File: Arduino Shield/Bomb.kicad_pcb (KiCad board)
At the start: 2 copper layers, 27.9 x 21.6 mm, 6 parts, among them J1 Digital/PWM, J2 I2C Out, J3 Power, J4 Logic, U1 ATtiny85

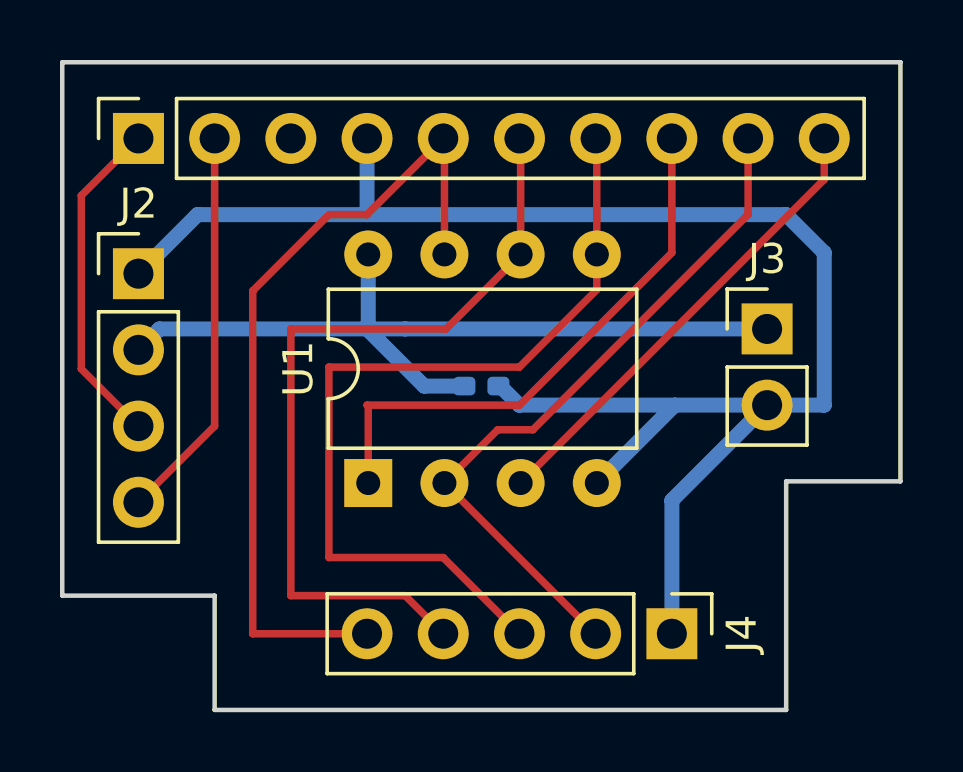
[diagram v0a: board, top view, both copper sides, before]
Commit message: Widened the pads of C1 in the arduino shield, switched the pinout of the i2c out, adjusted the size of the arduino shield board
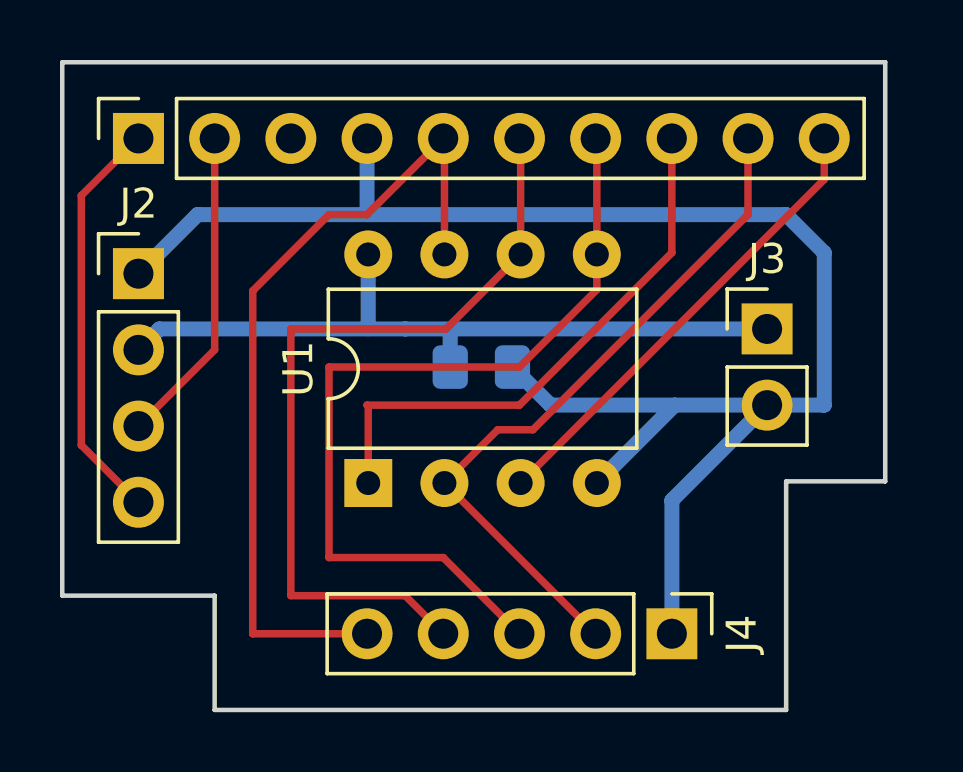
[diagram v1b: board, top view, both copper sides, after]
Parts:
- C1: footprint Capacitor_SMD:C_0402_1005Metric_Pad0.74x0.62mm_HandSolder -> Capacitor_SMD:C_0805_2012Metric_Pad1.18x1.45mm_HandSolder
- moved C1 0.63 mm to (129.2, 56.8)
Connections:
- J2 pad 3: /SCL/A5 -> /SDA/A4
- J2 pad 4: /SDA/A4 -> /SCL/A5
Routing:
- net +5V: track 27.7 -> 25.0 mm
- net /SDA/A4: track 13.2 -> 10.6 mm
- net /SCL/A5: track 11.2 -> 13.7 mm
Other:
- board size 27.9 x 21.6 mm -> 27.4 x 21.6 mm
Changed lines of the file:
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@@
       (net 2 "+5V") (pinfunction "Pin_2") (pintype "passive"))
     (pad "3" thru_hole oval (at 0 5.08) (size 1.7 1.7) (drill 1) (layers *.Cu *.Mask)
-      (net 4 "/SCL{slash}A5") (pinfunction "Pin_3") (pintype "passive"))
+      (net 3 "/SDA{slash}A4") (pinfunction "Pin_3") (pintype "passive"))
     (pad "4" thru_hole oval (at 0 7.62) (size 1.7 1.7) (drill 1) (layers *.Cu *.Mask)
-      (net 3 "/SDA{slash}A4") (pinfunction "Pin_4") (pintype "passive"))
+      (net 4 "/SCL{slash}A5") (pinfunction "Pin_4") (pintype "passive"))
     (model "${KICAD6_3DMODEL_DIR}/Connector_PinHeader_2.54mm.3dshapes/PinHeader_1x04_P2.54mm_Vertical.wrl"
       (offset (xyz 0 0 0))
@@
     )
   )
-  (footprint "Capacitor_SMD:C_0402_1005Metric_Pad0.74x0.62mm_HandSolder" (layer "B.Cu")
-    (at 129.21 57.455)
-    (descr "Capacitor SMD 0402 (1005 Metric), square (rectangular) end terminal, IPC_7351 nominal with elongated pad for handsoldering. (Body size source: IPC-SM-782 page 76, https://www.pcb-3d.com/wordpress/wp-content/uploads/ipc-sm-782a_amendment_1_and_2.pdf), generated with kicad-footprint-generator")
+  (footprint "Capacitor_SMD:C_0805_2012Metric_Pad1.18x1.45mm_HandSolder" (layer "B.Cu")
+    (at 129.21 56.82)
+    (descr "Capacitor SMD 0805 (2012 Metric), square (rectangular) end terminal, IPC_7351 nominal with elongated pad for handsoldering. (Body size source: IPC-SM-782 page 76, https://www.pcb-3d.com/wordpress/wp-content/uploads/ipc-sm-782a_amendment_1_and_2.pdf, https://docs.google.com/spreadsheets/d/1BsfQQcO9C6DZCsRaXUlFlo91Tg2WpOkGARC1WS5S8t0/edit?usp=sharing), generated with kicad-footprint-generator")
     (tags "capacitor handsolder")
     (property "Sheetfile" "Bomb.kicad_sch")
     (property "Sheetname" "")
     (attr smd)
-    (fp_text reference "C1" (at 0 1.16 180) (layer "B.SilkS")
+    (fp_text reference "C1" (at 0 1.68 180) (layer "B.SilkS")
       (effects (font (size 1 1) (thickness 0.15)) (justify mirror))
     )
-    (fp_text value "C" (at 0 -1.16 180) (layer "B.Fab") hide
+    (fp_text value "C" (at 0 -1.68 180) (layer "B.Fab")
       (effects (font (size 1 1) (thickness 0.15)) (justify mirror))
     )
     (fp_text user "${REFERENCE}" (at 0 0 180) (layer "B.Fab")
-      (effects (font (size 0.25 0.25) (thickness 0.04)) (justify mirror))
+      (effects (font (size 0.5 0.5) (thickness 0.08)) (justify mirror))
     )
-    (fp_line (start -0.115835 0.36) (end 0.115835 0.36) (layer "B.SilkS") (width 0.12))
-    (fp_line (start -0.115835 -0.36) (end 0.115835 -0.36) (layer "B.SilkS") (width 0.12))
-    (fp_line (start -1.08 -0.46) (end -1.08 0.46) (layer "B.CrtYd") (width 0.05))
-    (fp_line (start 1.08 0.46) (end 1.08 -0.46) (layer "B.CrtYd") (width 0.05))
-    (fp_line (start 1.08 -0.46) (end -1.08 -0.46) (layer "B.CrtYd") (width 0.05))
-    (fp_line (start -1.08 0.46) (end 1.08 0.46) (layer "B.CrtYd") (width 0.05))
-    (fp_line (start -0.5 0.25) (end 0.5 0.25) (layer "B.Fab") (width 0.1))
-    (fp_line (start 0.5 0.25) (end 0.5 -0.25) (layer "B.Fab") (width 0.1))
-    (fp_line (start 0.5 -0.25) (end -0.5 -0.25) (layer "B.Fab") (width 0.1))
-    (fp_line (start -0.5 -0.25) (end -0.5 0.25) (layer "B.Fab") (width 0.1))
-    (pad "1" smd roundrect (at -0.5675 0) (size 0.735 0.62) (layers "B.Cu" "B.Paste" "B.Mask") (roundrect_rratio 0.25)
+    (fp_line (start -0.261252 0.735) (end 0.261252 0.735) (layer "B.SilkS") (width 0.12))
+    (fp_line (start -0.261252 -0.735) (end 0.261252 -0.735) (layer "B.SilkS") (width 0.12))
+    (fp_line (start -1.88 0.98) (end 1.88 0.98) (layer "B.CrtYd") (width 0.05))
+    (fp_line (start 1.88 -0.98) (end -1.88 -0.98) (layer "B.CrtYd") (width 0.05))
+    (fp_line (start 1.88 0.98) (end 1.88 -0.98) (layer "B.CrtYd") (width 0.05))
+    (fp_line (start -1.88 -0.98) (end -1.88 0.98) (layer "B.CrtYd") (width 0.05))
+    (fp_line (start 1 0.625) (end 1 -0.625) (layer "B.Fab") (width 0.1))
+    (fp_line (start 1 -0.625) (end -1 -0.625) (layer "B.Fab") (width 0.1))
+    (fp_line (start -1 -0.625) (end -1 0.625) (layer "B.Fab") (width 0.1))
+    (fp_line (start -1 0.625) (end 1 0.625) (layer "B.Fab") (width 0.1))
+    (pad "1" smd roundrect (at -1.0375 0) (size 1.175 1.45) (layers "B.Cu" "B.Paste" "B.Mask") (roundrect_rratio 0.212766)
       (net 2 "+5V") (pintype "passive"))
-    (pad "2" smd roundrect (at 0.5675 0) (size 0.735 0.62) (layers "B.Cu" "B.Paste" "B.Mask") (roundrect_rratio 0.25)
+    (pad "2" smd roundrect (at 1.0375 0) (size 1.175 1.45) (layers "B.Cu" "B.Paste" "B.Mask") (roundrect_rratio 0.212766)
       (net 1 "GND") (pintype "passive"))
-    (model "${KICAD6_3DMODEL_DIR}/Capacitor_SMD.3dshapes/C_0402_1005Metric.wrl"
+    (model "${KICAD6_3DMODEL_DIR}/Capacitor_SMD.3dshapes/C_0805_2012Metric.wrl"
       (offset (xyz 0 0 0))
       (scale (xyz 1 1 1))
@@
   (gr_line (start 139.37 60.63) (end 139.37 68.25) (layer "Edge.Cuts") (width 0.15))
   (gr_line (start 115.24 64.44) (end 120.32 64.44) (layer "Edge.Cuts") (width 0.15))
-  (gr_line (start 143.18 46.66) (end 143.18 60.63) (layer "Edge.Cuts") (width 0.15))
+  (gr_line (start 142.672 46.66) (end 142.672 60.63) (layer "Edge.Cuts") (width 0.15))
   (gr_line (start 139.37 68.25) (end 120.32 68.25) (layer "Edge.Cuts") (width 0.15))
-  (gr_line (start 115.24 46.66) (end 143.18 46.66) (layer "Edge.Cuts") (width 0.15))
-  (gr_line (start 139.37 60.63) (end 143.18 60.63) (layer "Edge.Cuts") (width 0.15))
+  (gr_line (start 115.24 46.66) (end 142.672 46.66) (layer "Edge.Cuts") (width 0.15))
+  (gr_line (start 139.37 60.63) (end 142.672 60.63) (layer "Edge.Cuts") (width 0.15))
   (gr_text "-" (at 135.56 63.17 90) (layer "F.Fab")
     (effects (font (size 1 1) (thickness 0.15)))
@@
     (effects (font (size 1 1) (thickness 0.15)))
   )
+  (segment (start 131.5175 58.09) (end 130.2475 56.82) (width 0.5) (layer "B.Cu") (net 1))
   (segment (start 140.64 58.09) (end 138.735 58.09) (width 0.5) (layer "B.Cu") (net 1))
   (segment (start 139.37 51.74) (end 140.64 53.01) (width 0.5) (layer "B.Cu") (net 1))
   (segment (start 119.7475 51.74) (end 117.78 53.7075) (width 0.5) (layer "B.Cu") (net 1))
   (segment (start 135.56 61.265) (end 135.56 65.71) (width 0.5) (layer "B.Cu") (net 1))
-  (segment (start 130.4725 58.09) (end 129.8375 57.455) (width 0.5) (layer "B.Cu") (net 1))
   (segment (start 138.735 58.09) (end 135.56 61.265) (width 0.5) (layer "B.Cu") (net 1))
+  (segment (start 135.655504 58.09) (end 131.5175 58.09) (width 0.5) (layer "B.Cu") (net 1))
   (segment (start 125.4 51.74) (end 119.7475 51.74) (width 0.5) (layer "B.Cu") (net 1))
   (segment (start 125.4 51.74) (end 139.37 51.74) (width 0.5) (layer "B.Cu") (net 1))
   (segment (start 125.4 51.74) (end 125.4 49.2) (width 0.5) (layer "B.Cu") (net 1))
-  (segment (start 135.655504 58.09) (end 130.4725 58.09) (width 0.5) (layer "B.Cu") (net 1))
   (segment (start 140.64 53.01) (end 140.64 58.09) (width 0.5) (layer "B.Cu") (net 1))
   (segment (start 135.655504 58.09) (end 133.059261 60.686243) (width 0.5) (layer "B.Cu") (net 1))
   (segment (start 138.735 58.09) (end 135.655504 58.09) (width 0.5) (layer "B.Cu") (net 1))
   (segment (start 125.4 55.55) (end 118.4775 55.55) (width 0.5) (layer "B.Cu") (net 2))
-  (segment (start 138.735 55.55) (end 126.67 55.55) (width 0.5) (layer "B.Cu") (net 2))
-  (segment (start 127.305 57.455) (end 128.5825 57.455) (width 0.5) (layer "B.Cu") (net 2))
+  (segment (start 128.1725 56.82) (end 128.1725 55.5715) (width 0.5) (layer "B.Cu") (net 2))
+  (segment (start 128.194 55.55) (end 126.67 55.55) (width 0.5) (layer "B.Cu") (net 2))
   (segment (start 125.439261 53.066243) (end 125.439261 55.510739) (width 0.5) (layer "B.Cu") (net 2))
-  (segment (start 125.4 55.55) (end 127.305 57.455) (width 0.5) (layer "B.Cu") (net 2))
+  (segment (start 128.1725 55.5715) (end 128.194 55.55) (width 0.2) (layer "B.Cu") (net 2))
   (segment (start 118.4775 55.55) (end 117.78 56.2475) (width 0.5) (layer "B.Cu") (net 2))
+  (segment (start 138.735 55.55) (end 128.194 55.55) (width 0.5) (layer "B.Cu") (net 2))
   (segment (start 125.439261 55.510739) (end 125.478522 55.55) (width 0.25) (layer "B.Cu") (net 2))
   (segment (start 125.439261 55.510739) (end 125.4 55.55) (width 0.25) (layer "B.Cu") (net 2))
   (segment (start 125.478522 55.55) (end 126.67 55.55) (width 0.5) (layer "B.Cu") (net 2))
-  (segment (start 120.32 49.2) (end 120.32 58.7875) (width 0.25) (layer "F.Cu") (net 3))
-  (segment (start 120.32 58.7875) (end 117.78 61.3275) (width 0.25) (layer "F.Cu") (net 3))
+  (segment (start 120.32 56.2475) (end 117.78 58.7875) (width 0.25) (layer "F.Cu") (net 3))
+  (segment (start 120.32 49.2) (end 120.32 56.2475) (width 0.25) (layer "F.Cu") (net 3))
+  (segment (start 115.875 51.105) (end 115.875 59.4225) (width 0.25) (layer "F.Cu") (net 4))
   (segment (start 117.78 49.2) (end 115.875 51.105) (width 0.25) (layer "F.Cu") (net 4))
-  (segment (start 115.875 56.8825) (end 117.78 58.7875) (width 0.25) (layer "F.Cu") (net 4))
-  (segment (start 115.875 51.105) (end 115.875 56.8825) (width 0.25) (layer "F.Cu") (net 4))
+  (segment (start 115.875 59.4225) (end 117.78 61.3275) (width 0.25) (layer "F.Cu") (net 4))
   (segment (start 125.4 51.74) (end 124.13 51.74) (width 0.25) (layer "F.Cu") (net 5))
   (segment (start 121.59 65.71) (end 125.4 65.71) (width 0.25) (layer "F.Cu") (net 5))
